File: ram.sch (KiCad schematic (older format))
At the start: 10 parts, among them U5 4416, U6 4416, U7 74LS257, U8 74LS257

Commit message: Add 16/64k RAM switch
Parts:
- added JP1: JP_RAMSIZE1, Connector_PinHeader_2.54mm:PinHeader_1x03_P2.54mm_Vertical, symbol Connector:Conn_01x03_Male
- added JP2: JP_RAMSIZE2, Connector_PinHeader_2.54mm:PinHeader_1x03_P2.54mm_Vertical, symbol Connector:Conn_01x03_Male
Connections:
- net VCC: now also JP1.1 (Pin_1), JP2.1 (Pin_1); no longer U7.2 (I0a), U8.14 (I0c)
- new net: JP2.2 (Pin_2), U8.14 (I0c)
- new net: JP1.2 (Pin_2), U7.2 (I0a)
- new net a14: JP2.3 (Pin_3)
- new net a15: JP1.3 (Pin_3)
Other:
- note added: "JP1/2 are a 16kB/64kB\nRAM Switch Mod. Use\n4464 chips instead of 4416."
- note added: "Yes, RP3/4 have this\nweird pin numbering,\nmost likely in order to\nmake routing easier"
- note removed: "Yes, RP3/4 have this\nweird pin numbering..."
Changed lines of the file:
@@
 Sheet 4 12
 Title "LittleSixteen"
-Date "2021-07-20"
+Date "2021-11-06"
 Rev "2git"
 Comp "SukkoPera"
@@
 Wire Wire Line
 	1905 2690 2420 2690
-$Comp
-L power:VCC #PWR0118
-U 1 1 5E691A04
-P 3320 1130
-F 0 "#PWR0118" H 3320 980 50  0001 C CNN
-F 1 "VCC" H 3337 1303 50  0000 C CNN
-F 2 "" H 3320 1130 50  0001 C CNN
-F 3 "" H 3320 1130 50  0001 C CNN
-	1    3320 1130
-	1    0    0    -1
-$EndComp
 Wire Wire Line
 	3475 1490 3320 1490
@@
 MUX
 Wire Bus Line
-	2565 1490 2050 1490
-Text GLabel 2050 1490 0    50   Input ~ 0
+	2565 1160 2050 1160
+Text GLabel 2050 1160 0    50   Input ~ 0
 a[0..15]
 $Comp
@@
 L power:VCC #PWR0120
 U 1 1 5E710070
-P 3320 3870
-F 0 "#PWR0120" H 3320 3720 50  0001 C CNN
-F 1 "VCC" H 3337 4043 50  0000 C CNN
-F 2 "" H 3320 3870 50  0001 C CNN
-F 3 "" H 3320 3870 50  0001 C CNN
-	1    3320 3870
+P 3585 3790
+F 0 "#PWR0120" H 3585 3640 50  0001 C CNN
+F 1 "VCC" H 3602 3963 50  0000 C CNN
+F 2 "" H 3585 3790 50  0001 C CNN
+F 3 "" H 3585 3790 50  0001 C CNN
+	1    3585 3790
 	1    0    0    -1
 $EndComp
@@
 	1    0    0    -1
 $EndComp
-Text Notes 2720 3580 0    50   ~ 0
+Text Notes 2715 3550 0    50   ~ 0
 U7 and U8 can either be 74x157 or 74x257,\nsince they are permanently enabled
 Wire Wire Line
@@
 	0    1    1    0
 $EndComp
-Text Notes 4810 3585 1    50   ~ 0
-Yes, RP3/4 have this\nweird pin numbering...
+Text Notes 4915 3675 1    50   ~ 0
+Yes, RP3/4 have this\nweird pin numbering,\nmost likely in order to\nmake routing easier
 $Comp
 L Device:C C35
@@
 Wire Wire Line
 	3380 6525 3760 6525
+$Comp
+L Connector:Conn_01x03_Male JP2
+U 1 1 61451C3E
+P 3320 3670
+F 0 "JP2" V 3382 3482 50  0000 R CNN
+F 1 "JP_RAMSIZE2" V 3473 3482 50  0000 R CNN
+F 2 "Connector_PinHeader_2.54mm:PinHeader_1x03_P2.54mm_Vertical" H 3320 3670 50  0001 C CNN
+F 3 "~" H 3320 3670 50  0001 C CNN
+	1    3320 3670
+	0    1    1    0
+$EndComp
+Wire Wire Line
+	3420 3870 3420 4000
+Wire Wire Line
+	3420 4000 3585 4000
+Wire Wire Line
+	3585 4000 3585 3790
+Wire Wire Line
+	3220 3870 3220 4000
+Wire Wire Line
+	3220 4000 2665 4000
+Entry Wire Line
+	2565 3900 2665 4000
+Text Label 2865 4000 0    60   ~ 0
+a14
+$Comp
+L power:VCC #PWR0118
+U 1 1 6147AF8D
+P 3585 1050
+F 0 "#PWR0118" H 3585 900 50  0001 C CNN
+F 1 "VCC" H 3602 1223 50  0000 C CNN
+F 2 "" H 3585 1050 50  0001 C CNN
+F 3 "" H 3585 1050 50  0001 C CNN
+	1    3585 1050
+	1    0    0    -1
+$EndComp
+$Comp
+L Connector:Conn_01x03_Male JP1
+U 1 1 6147B280
+P 3320 930
+F 0 "JP1" V 3382 742 50  0000 R CNN
+F 1 "JP_RAMSIZE1" V 3473 742 50  0000 R CNN
+F 2 "Connector_PinHeader_2.54mm:PinHeader_1x03_P2.54mm_Vertical" H 3320 930 50  0001 C CNN
+F 3 "~" H 3320 930 50  0001 C CNN
+	1    3320 930
+	0    1    1    0
+$EndComp
+Wire Wire Line
+	3420 1130 3420 1260
+Wire Wire Line
+	3420 1260 3585 1260
+Wire Wire Line
+	3585 1260 3585 1050
+Wire Wire Line
+	3220 1130 3220 1260
+Wire Wire Line
+	3220 1260 2665 1260
+Entry Wire Line
+	2565 1160 2665 1260
+Text Label 2865 1260 0    60   ~ 0
+a15
+Text Notes 3730 1130 0    50   ~ 0
+JP1/2 are a 16kB/64kB\nRAM Switch Mod. Use\n4464 chips instead of 4416.
 Wire Bus Line
 	5815 1220 5815 3440
@@
 	8985 2140 8985 5230
 Wire Bus Line
-	2565 1490 2565 5130
+	2565 1160 2565 5130
 $EndSCHEMATC

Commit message: Add a way to disable internal RAM from expansion connector
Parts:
- added R99: 10k, Resistor_THT:R_Axial_DIN0207_L6.3mm_D2.5mm_P5.08mm_Vertical, symbol Device:R
- added U12: 74LS02, Package_DIP:DIP-14_W7.62mm_Socket_LongPads, symbol 74xx:74LS02
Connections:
- net GND: no longer U7.15 (E), U8.15 (E)
- net VCC: now also R99.1
- new net RAMEN: R99.2, U12.11, U12.12
- new net ~ramen: U12.13, U7.15 (E), U8.15 (E)
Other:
- note added: "We make use of a spare gate to fix the\neternal problem of external RAM\nexpansions not working, which is due to\nthe impossibility of disabling the internal\nRAM. This should do it, just ground the Z\npin and the internal RAM will disappear."
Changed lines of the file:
@@
 Sheet 4 12
 Title "LittleSixteen"
-Date "2021-11-06"
+Date "2021-11-08"
 Rev "2git"
 Comp "SukkoPera"
@@
 a0
 Wire Wire Line
-	3475 2790 3320 2790
-Wire Wire Line
 	2665 1590 3475 1590
 Text Label 2865 2490 0    60   ~ 0
@@
 	2665 2390 3475 2390
 Wire Wire Line
-	1905 2690 2420 2690
+	2320 2690 2420 2690
 Wire Wire Line
 	3475 1490 3320 1490
 Wire Wire Line
 	3320 1490 3320 1130
-Text GLabel 1905 2690 0    50   Input ~ 0
+Text GLabel 2320 2690 0    50   Input ~ 0
 MUX
 Wire Bus Line
-	2565 1160 2050 1160
-Text GLabel 2050 1160 0    50   Input ~ 0
+	2565 1160 2350 1160
+Text GLabel 2350 1160 0    50   Input ~ 0
 a[0..15]
-$Comp
-L power:GND #PWR0119
-U 1 1 5E6F60AB
-P 3320 3160
-F 0 "#PWR0119" H 3320 2910 50  0001 C CNN
-F 1 "GND" H 3325 2987 50  0000 C CNN
-F 2 "" H 3320 3160 50  0001 C CNN
-F 3 "" H 3320 3160 50  0001 C CNN
-	1    3320 3160
-	1    0    0    -1
-$EndComp
-Wire Wire Line
-	3320 2790 3320 3160
 Entry Wire Line
 	2565 4230 2665 4330
 Text Label 2865 4330 0    60   ~ 0
 a4
-Wire Wire Line
-	3475 5530 3320 5530
 Wire Wire Line
 	2665 4330 3475 4330
@@
 	1    0    0    -1
 $EndComp
-$Comp
-L power:GND #PWR0121
-U 1 1 5E710080
-P 3320 5900
-F 0 "#PWR0121" H 3320 5650 50  0001 C CNN
-F 1 "GND" H 3325 5727 50  0000 C CNN
-F 2 "" H 3320 5900 50  0001 C CNN
-F 3 "" H 3320 5900 50  0001 C CNN
-	1    3320 5900
-	1    0    0    -1
-$EndComp
-Wire Wire Line
-	3320 5530 3320 5900
 Entry Wire Line
 	2565 4130 2665 4230
@@
 Text Notes 3730 1130 0    50   ~ 0
 JP1/2 are a 16kB/64kB\nRAM Switch Mod. Use\n4464 chips instead of 4416.
+Text GLabel 965  2690 0    50   Input ~ 0
+RAMEN
+$Comp
+L 74xx:74LS02 U?
+U 4 1 618ABE98
+P 1535 2790
+AR Path="/5EE7AAEB/618ABE98" Ref="U?"  Part="4"
+AR Path="/5EACE220/618ABE98" Ref="U?"  Part="4"
+AR Path="/5E4A465A/618ABE98" Ref="U12"  Part="4"
+F 0 "U12" H 1535 3115 50  0000 C CNN
+F 1 "74LS02" H 1535 3024 50  0000 C CNN
+F 2 "Package_DIP:DIP-14_W7.62mm_Socket_LongPads" H 1535 2790 50  0001 C CNN
+F 3 "http://www.ti.com/lit/gpn/sn74ls02" H 1535 2790 50  0001 C CNN
+	4    1535 2790
+	1    0    0    -1
+$EndComp
+Wire Wire Line
+	965  2690 1135 2690
+Wire Wire Line
+	1135 2690 1135 2890
+Wire Wire Line
+	1135 2890 1235 2890
+Connection ~ 1135 2690
+Wire Wire Line
+	1135 2690 1235 2690
+Wire Wire Line
+	1835 2790 2320 2790
+Wire Wire Line
+	2320 2790 2320 5530
+Connection ~ 2320 2790
+Wire Wire Line
+	2320 2790 3475 2790
+Wire Wire Line
+	2320 5530 3475 5530
+$Comp
+L Device:R R99
+U 1 1 61920791
+P 1135 2350
+F 0 "R99" H 1205 2396 50  0000 L CNN
+F 1 "10k" H 1205 2305 50  0000 L CNN
+F 2 "Resistor_THT:R_Axial_DIN0207_L6.3mm_D2.5mm_P5.08mm_Vertical" V 1065 2350 50  0001 C CNN
+F 3 "~" H 1135 2350 50  0001 C CNN
+	1    1135 2350
+	1    0    0    -1
+$EndComp
+Wire Wire Line
+	1135 2500 1135 2690
+$Comp
+L power:VCC #PWR0119
+U 1 1 61928882
+P 1135 2100
+F 0 "#PWR0119" H 1135 1950 50  0001 C CNN
+F 1 "VCC" H 1152 2273 50  0000 C CNN
+F 2 "" H 1135 2100 50  0001 C CNN
+F 3 "" H 1135 2100 50  0001 C CNN
+	1    1135 2100
+	1    0    0    -1
+$EndComp
+Wire Wire Line
+	1135 2100 1135 2200
+Text Label 1845 2790 0    50   ~ 0
+~ramen
 Wire Bus Line
 	5815 1220 5815 3440
@@
 Wire Bus Line
 	2565 1160 2565 5130
+Text Notes 660  3570 0    50   ~ 0
+We make use of a spare gate to fix the\neternal problem of external RAM\nexpansions not working, which is due to\nthe impossibility of disabling the internal\nRAM. This should do it, just ground the Z\npin and the internal RAM will disappear.
 $EndSCHEMATC

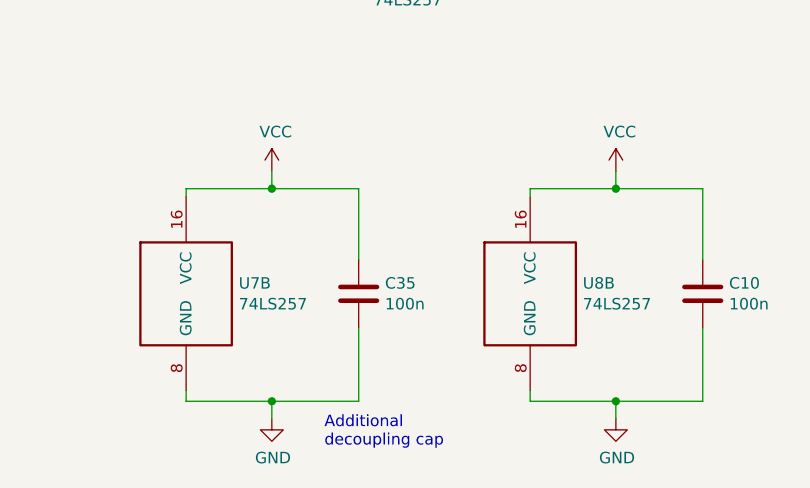
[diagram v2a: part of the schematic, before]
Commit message: Rename extra caps and switch to full THT power circuit Well, there's one SMD component, but it's optional :)
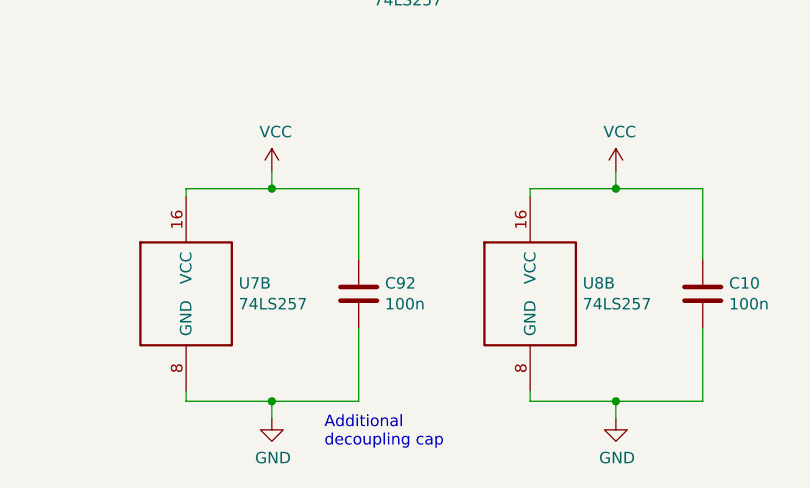
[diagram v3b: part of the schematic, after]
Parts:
- renumbered C35 to C92
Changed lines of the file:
@@
 Yes, RP3/4 have this\nweird pin numbering,\nmost likely in order to\nmake routing easier
 $Comp
-L Device:C C35
+L Device:C C92
 U 1 1 611A31E9
 P 3760 6985
-F 0 "C35" H 3875 7031 50  0000 L CNN
+F 0 "C92" H 3875 7031 50  0000 L CNN
 F 1 "100n" H 3875 6940 50  0000 L CNN
 F 2 "Capacitor_THT:C_Disc_D8.0mm_W2.5mm_P5.00mm" H 3798 6835 50  0001 C CNN
@@
 Text Label 1845 2790 0    50   ~ 0
 ~ramen
+Text Notes 660  3570 0    50   ~ 0
+We make use of a spare gate to fix the\neternal problem of external RAM\nexpansions not working, which is due to\nthe impossibility of disabling the internal\nRAM. This should do it, just ground the Z\npin and the internal RAM will disappear.
 Wire Bus Line
 	5815 1220 5815 3440
@@
 Wire Bus Line
 	2565 1160 2565 5130
-Text Notes 660  3570 0    50   ~ 0
-We make use of a spare gate to fix the\neternal problem of external RAM\nexpansions not working, which is due to\nthe impossibility of disabling the internal\nRAM. This should do it, just ground the Z\npin and the internal RAM will disappear.
 $EndSCHEMATC

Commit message: Improve power zones
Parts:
- RP3, RP4: Notes (none) -> Independent
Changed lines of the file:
@@
 F 2 "Resistor_THT:R_Array_SIP8" V 4810 1950 50  0001 C CNN
 F 3 "" H 4885 1950 50  0001 C CNN
+F 4 "Independent" H 4745 1950 50  0001 C CNN "Notes"
 	1    4745 1950
 	0    1    1    0
@@
 F 2 "Resistor_THT:R_Array_SIP8" V 4810 4690 50  0001 C CNN
 F 3 "" H 4885 4690 50  0001 C CNN
+F 4 "Independent" H 4745 4690 50  0001 C CNN "Notes"
 	1    4745 4690
 	0    1    1    0

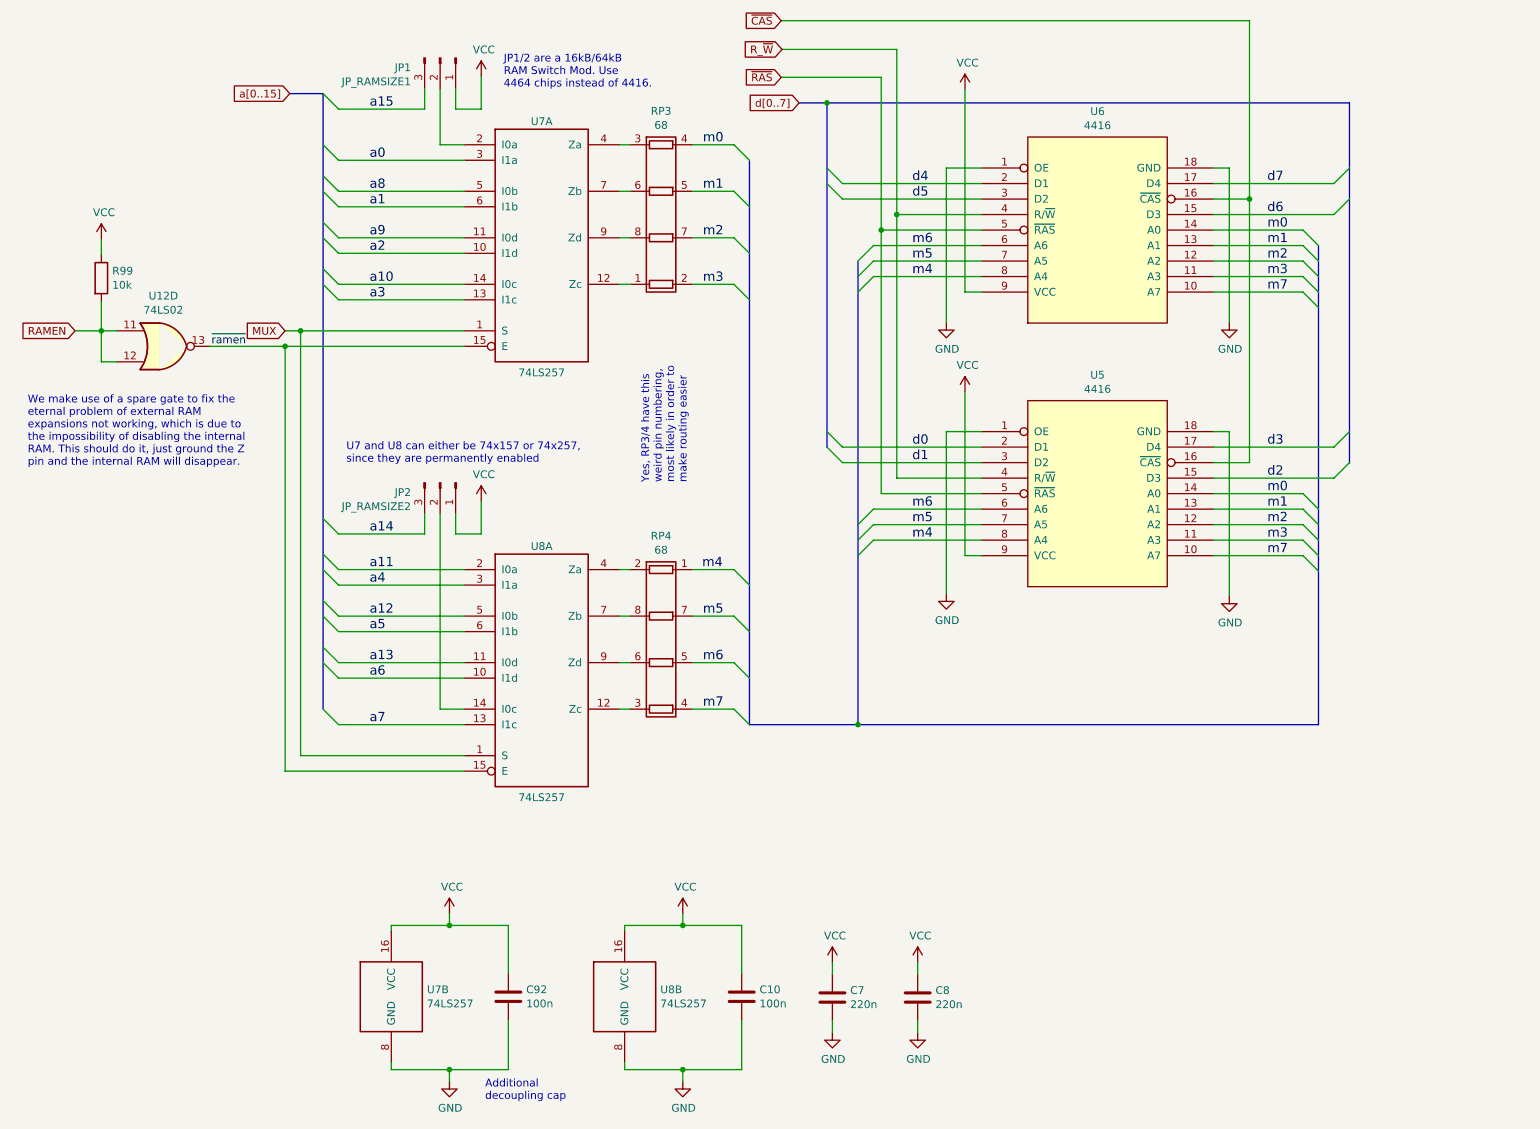
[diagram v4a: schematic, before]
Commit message: /RAMEN should go to the RAMs' /OE, not to the MUXs'...
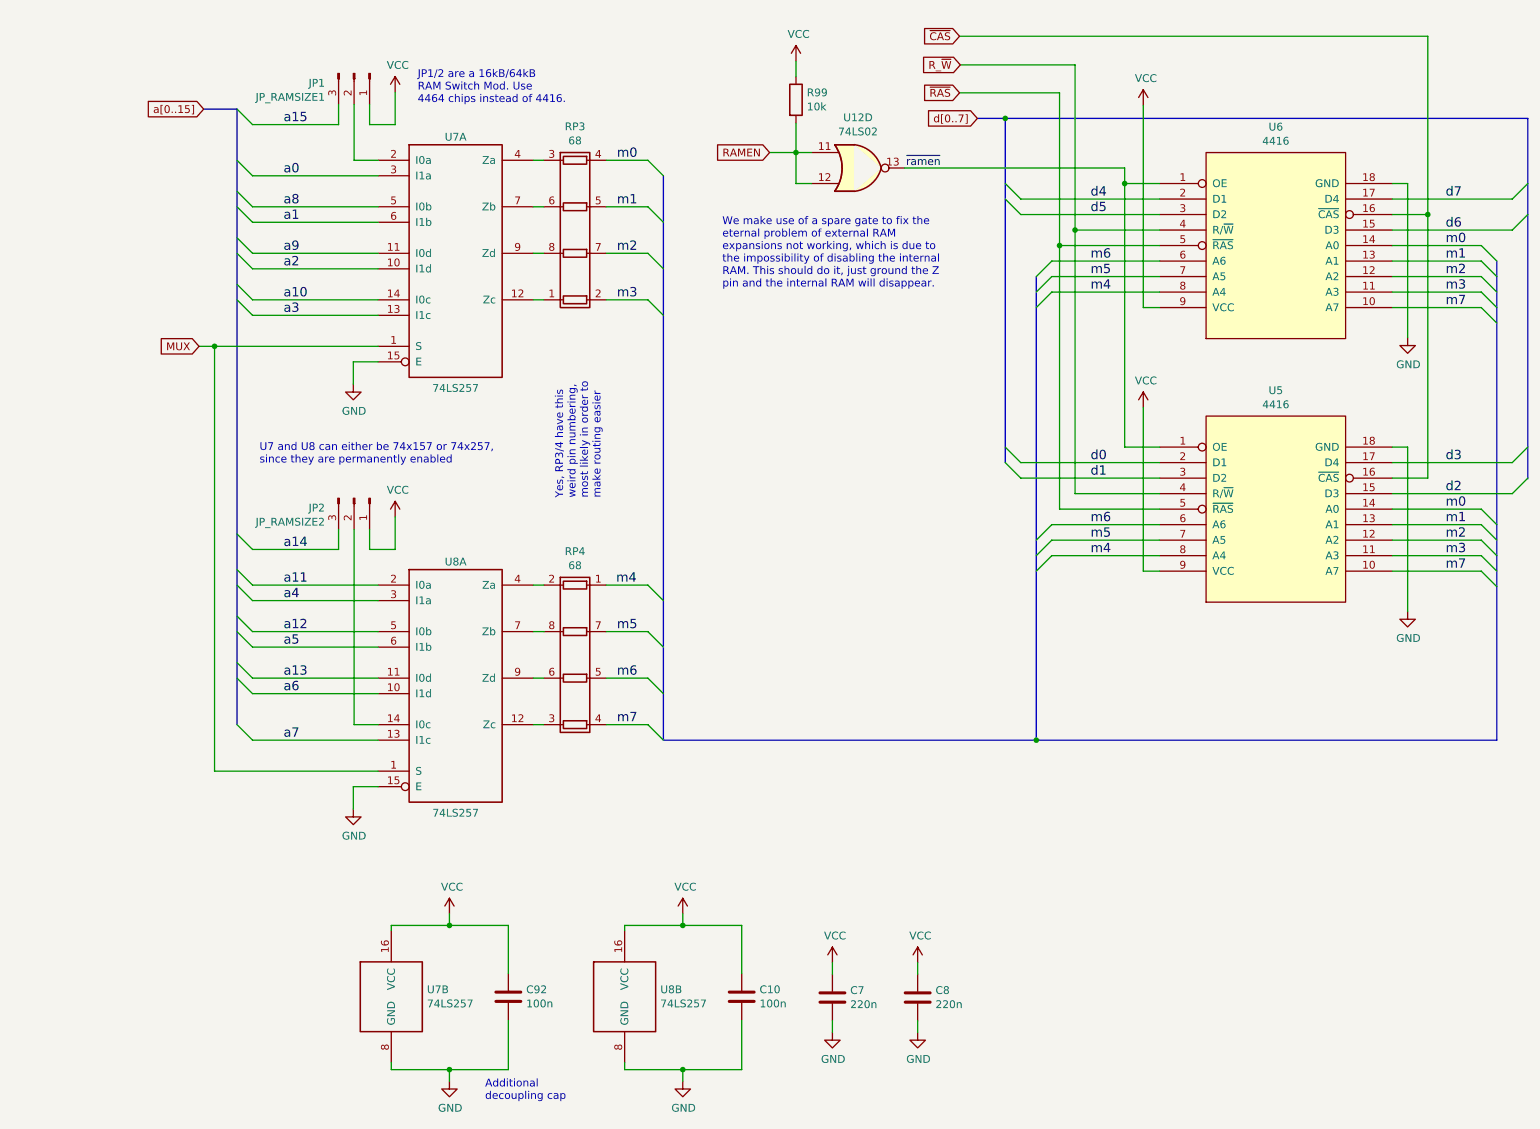
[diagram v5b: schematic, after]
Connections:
- net GND: now also U7.15 (E), U8.15 (E); no longer U5.1 (OE), U6.1 (OE)
- net ~ramen: now also U5.1 (OE), U6.1 (OE); no longer U7.15 (E), U8.15 (E)
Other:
- moved on the sheet: JP1, JP2, R99, RP3, RP4, U12D, U5, U6, U7A, U8A
